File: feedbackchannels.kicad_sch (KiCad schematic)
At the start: 93 parts

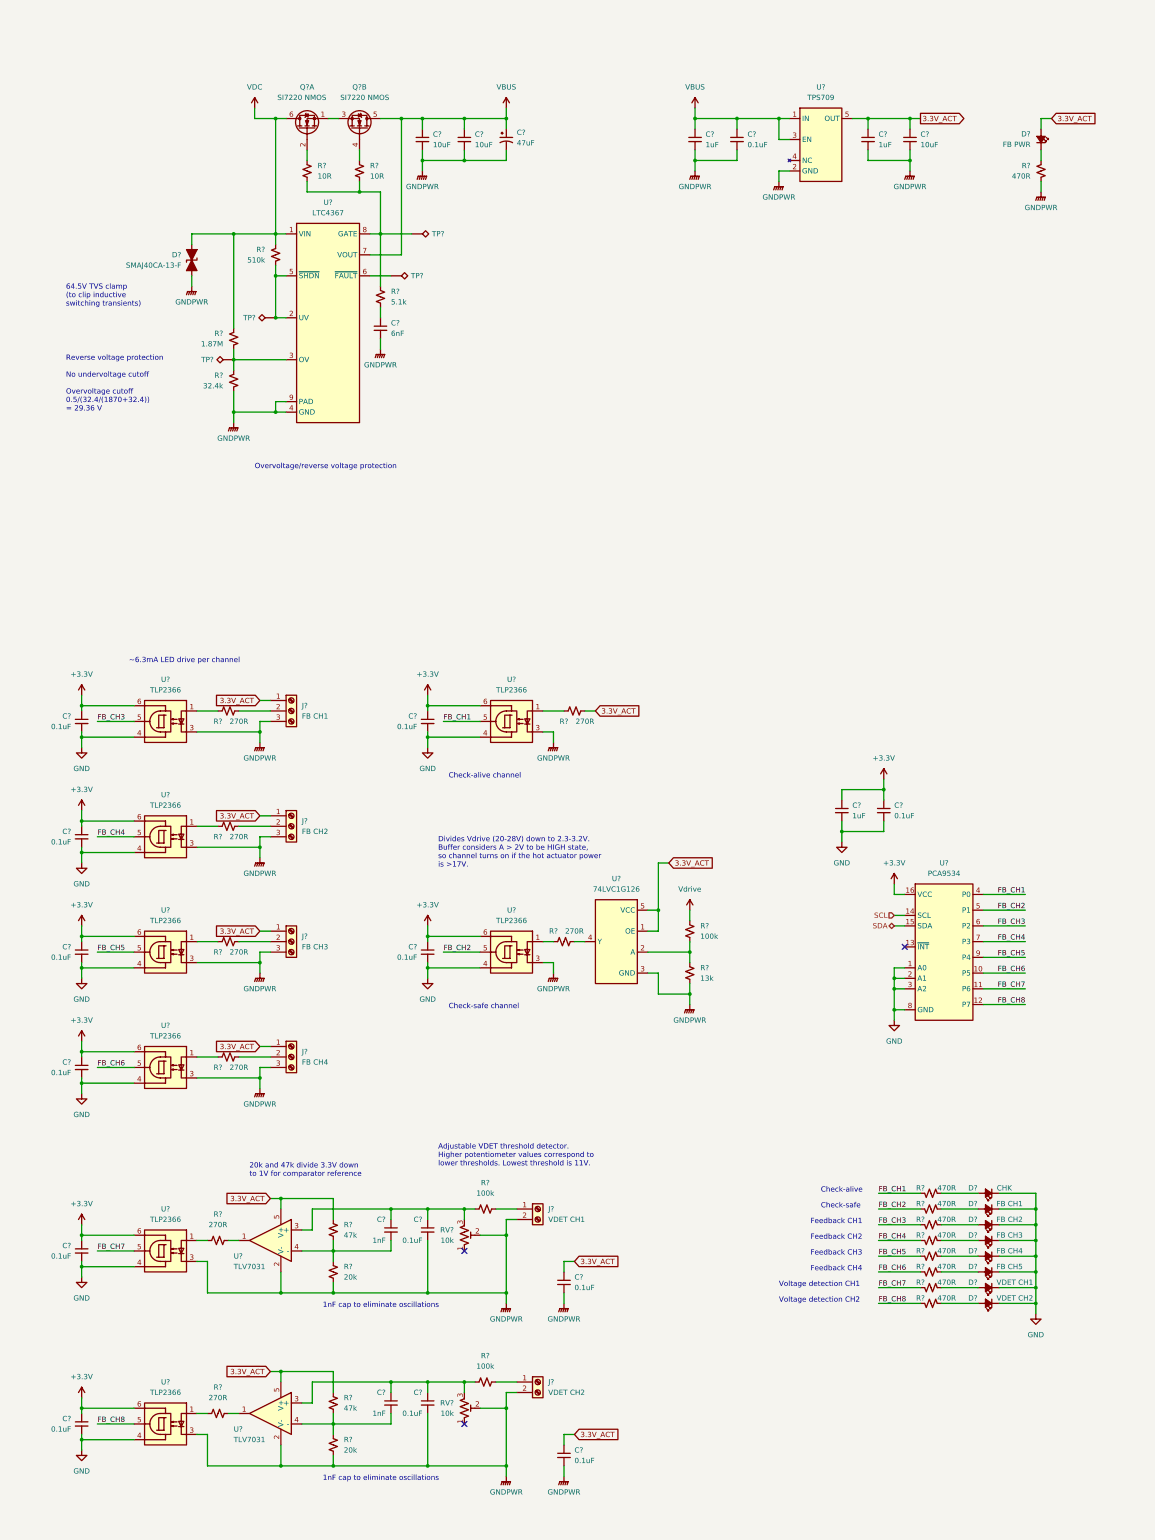
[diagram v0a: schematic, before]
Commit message: Replaced hot-side feedback LDO with buck converter
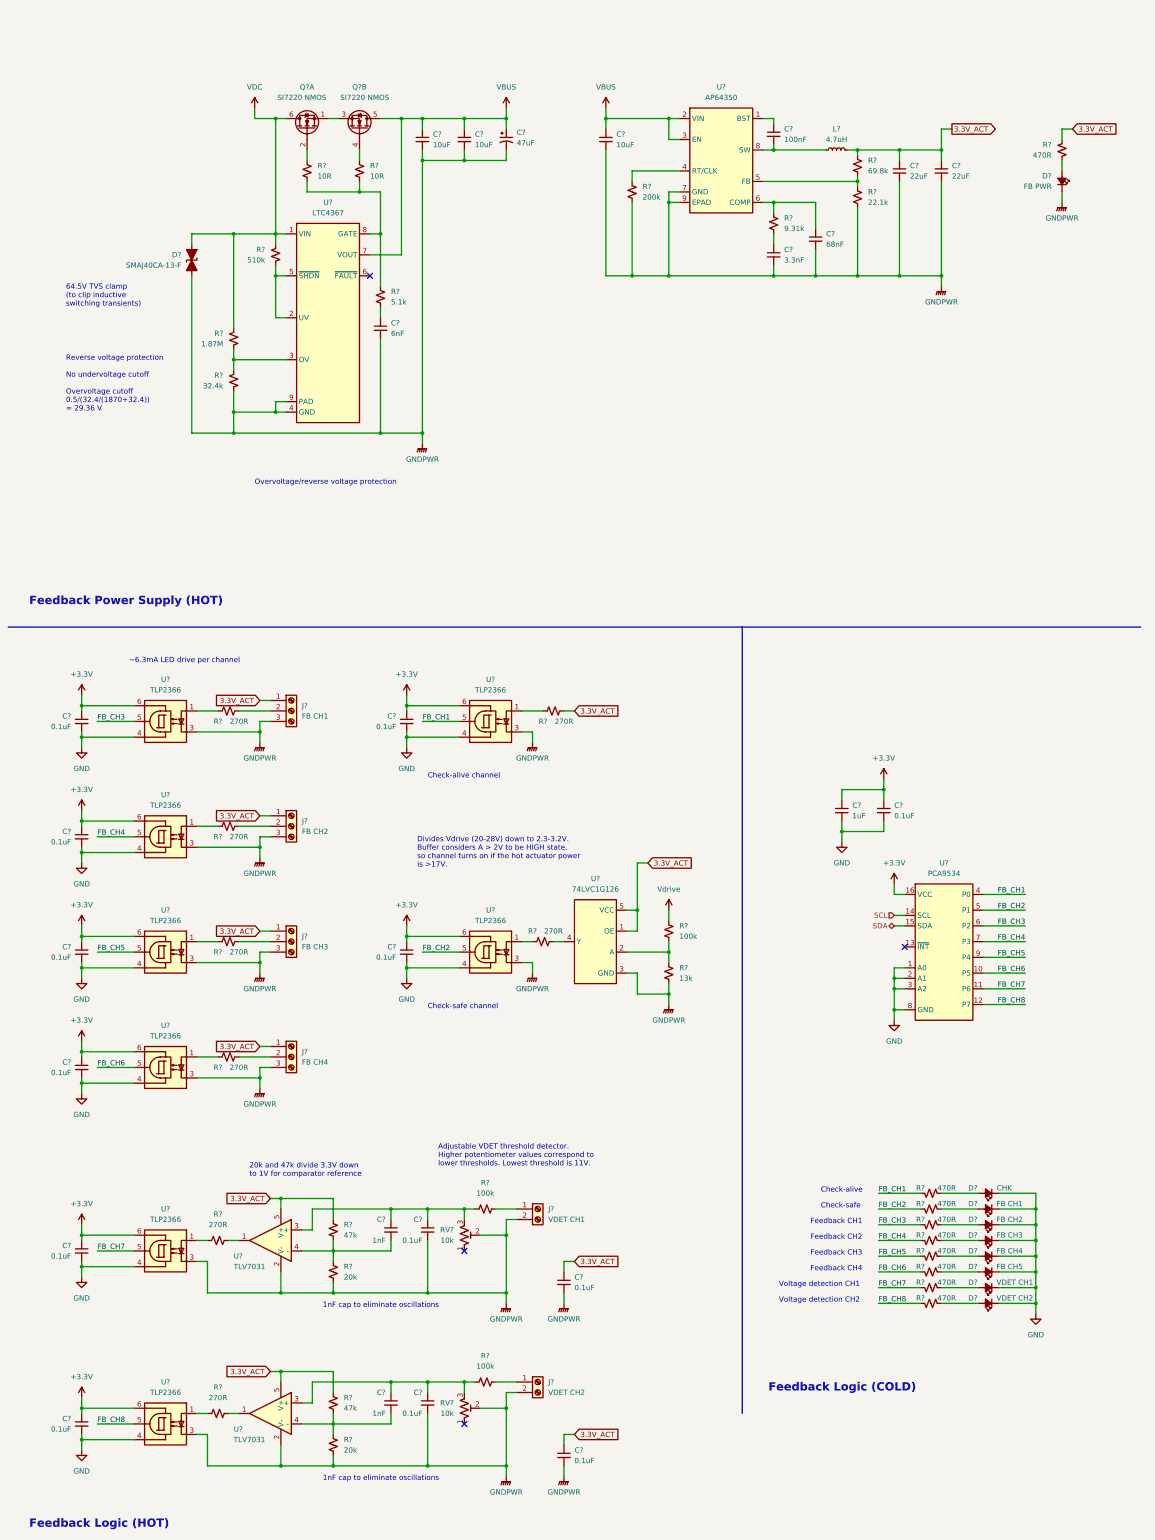
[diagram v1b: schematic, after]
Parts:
- removed C?: 10uF, Capacitor_SMD:C_0603_1608Metric, symbol Device:C_Small
- removed C? (x2): 1uF, Capacitor_SMD:C_0603_1608Metric, symbol Device:C_Small
- removed C?: 0.1uF, Capacitor_SMD:C_0603_1608Metric, symbol Device:C_Small
- removed TP? (x4): TestPoint_Alt, TestPoint:TestPoint_Pad_D2.0mm, symbol Connector:TestPoint_Alt
- removed U?: TPS709, Package_TO_SOT_SMD:SOT-23-5, symbol actuation:TPS709
- added C?: 10uF, symbol Device:C_Small
- added C?: 100nF, symbol Device:C_Small
- added C?: 68nF, symbol Device:C_Small
- added C?: 3.3nF, symbol Device:C_Small
- added C? (x2): 22uF, symbol Device:C_Small
- added L?: 4.7uH, symbol Device:L_Small
- added R?: 200k, symbol Device:R_Small_US
- added R?: 69.8k, symbol Device:R_Small_US
- added R?: 22.1k, symbol Device:R_Small_US
- added R?: 9.31k, symbol Device:R_Small_US
- added U?: AP64350, Package_SO:SOIC-8-1EP_3.9x4.9mm_P1.27mm_EP2.62x3.51mm, symbol actuation:AP64350
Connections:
- net 3.3V_ACT: now also R?.1, C?.1, C?.1, L?.2, R?.1; no longer D?.2 (A)
- net GNDPWR: now also D?.1 (K), C?.2, C?.2, C?.2, C?.2, C?.2, R?.2, R?.2, U?.7 (GND), U?.9 (EPAD); no longer R?.2
- net VBUS: now also C?.1, U?.2 (VIN), U?.3 (EN)
- new net: C?.2, L?.1, U?.8 (SW)
- new net: C?.1, U?.1 (BST)
- new net: R?.1, U?.4 (RT/CLK)
- new net: R?.1, R?.2, U?.5 (FB)
- new net: C?.1, R?.1, U?.6 (COMP)
- new net: C?.1, R?.2
- new net: D?.2 (A), R?.2
- no-connect marks 3 -> 4
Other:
- note added: "Feedback Logic (COLD)"
- note added: "Feedback Logic (HOT)"
- note added: "Feedback Power Supply (HOT)"
- moved on the sheet: C?, D?, R?, U?

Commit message: Reorganizing schematic
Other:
- moved on the sheet: C?, D?, J?, L?, Q?A, Q?B, R?, RV?, U?
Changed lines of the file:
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@@
 (kicad_sch (version 20211123) (generator eeschema)
-  (paper "User" 299.999 399.999)
+  (paper "User" 299.999 380.009)

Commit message: More reorganizing
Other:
- note added: "Feedback Isolators"
- note added: "Feedback Logic"
- note added: "Feedback Power Supply"
- note removed: "Feedback Logic (COLD)"
- note removed: "Feedback Logic (HOT)"
- note removed: "Feedback Power Supply (HOT)"

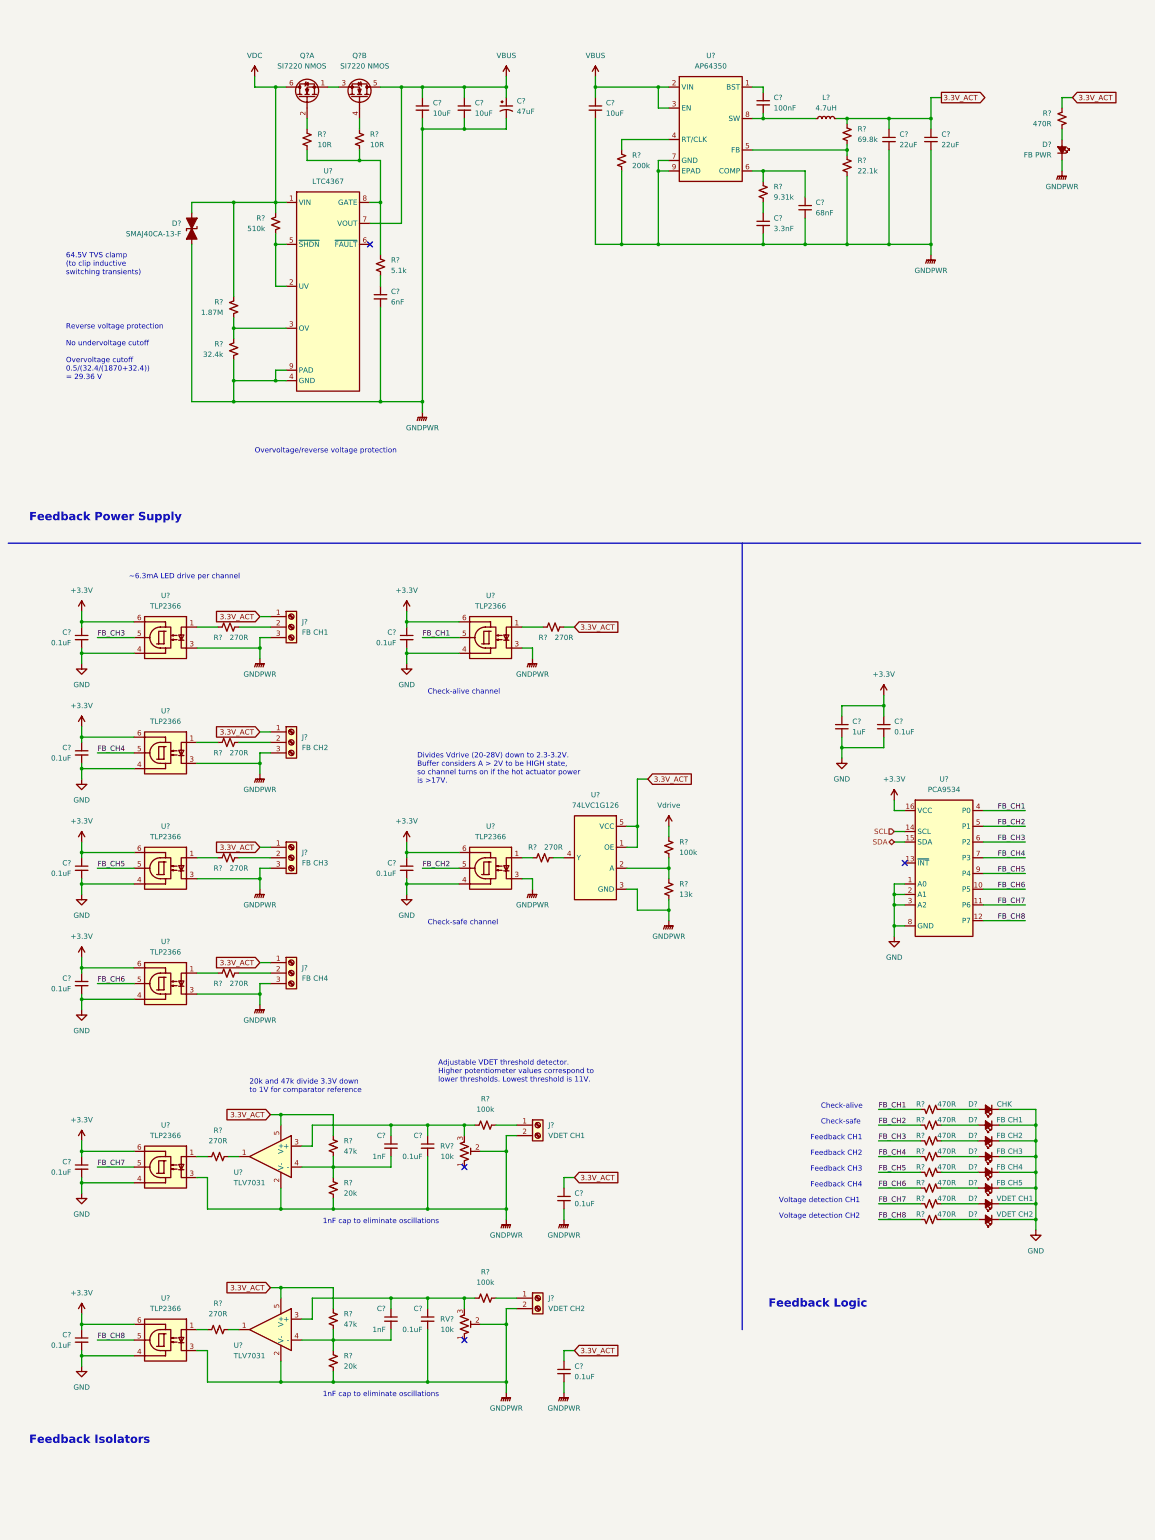
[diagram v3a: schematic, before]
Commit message: Terminal block part selections
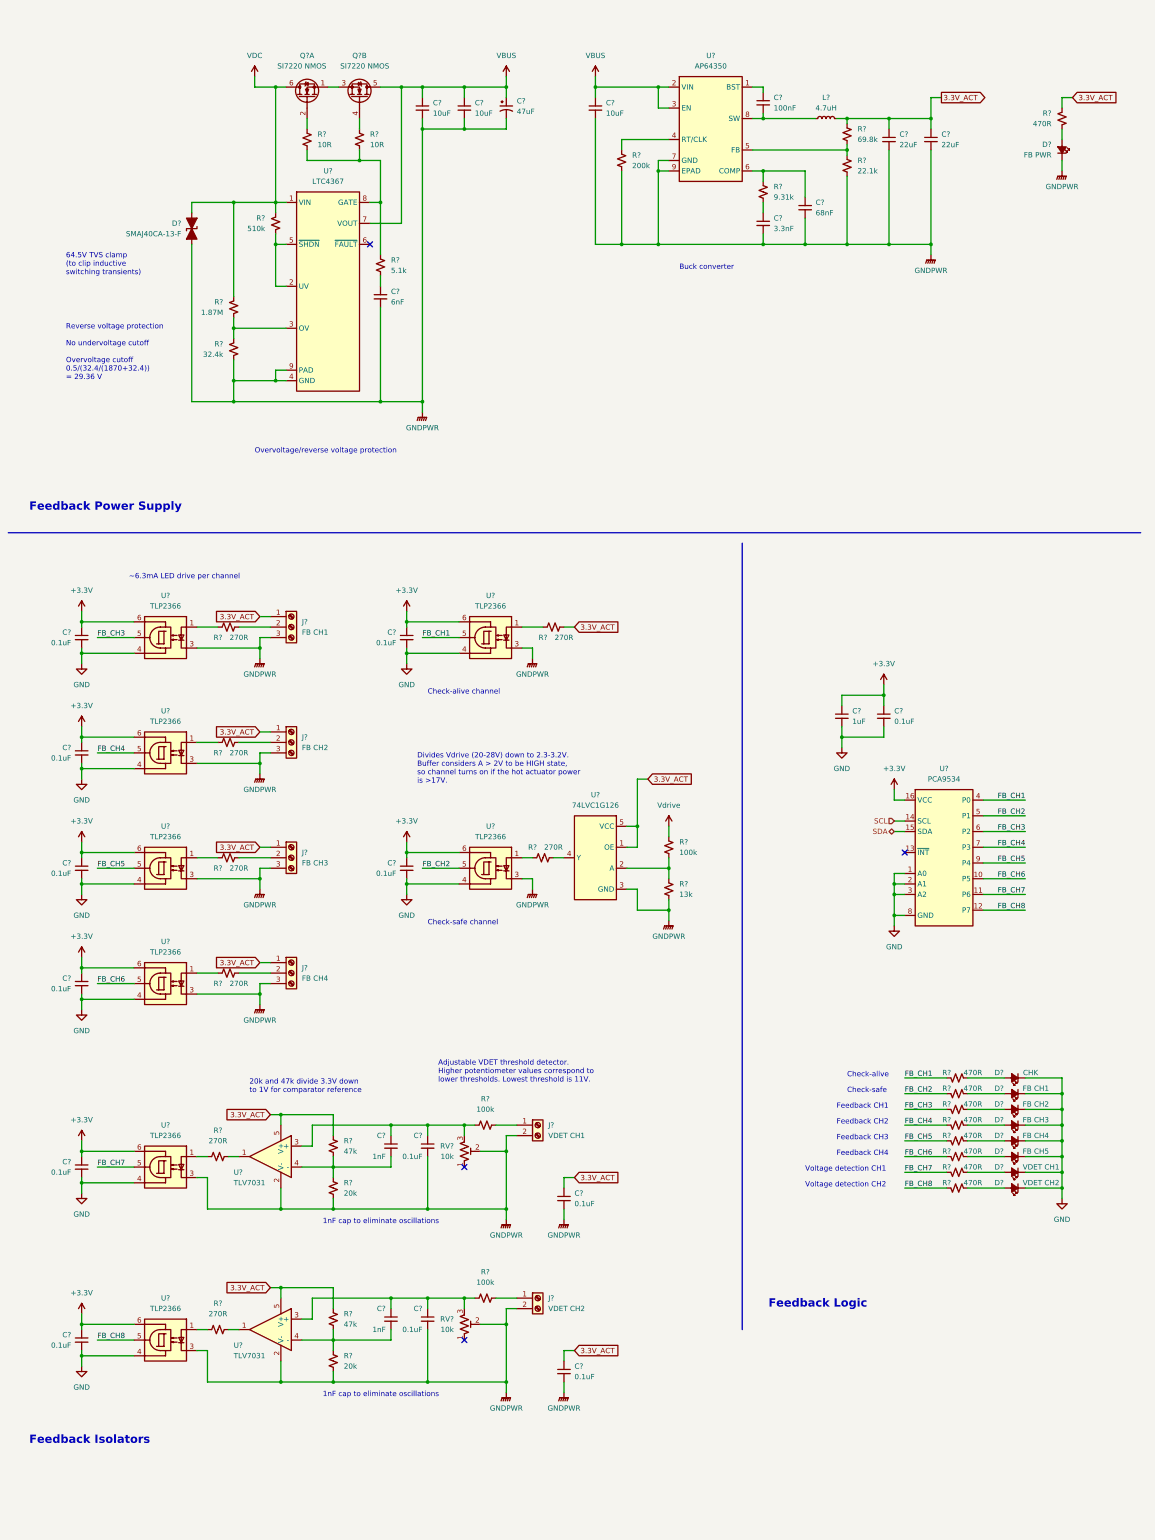
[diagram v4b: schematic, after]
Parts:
- removed J?: FB CH2, symbol Connector:Screw_Terminal_01x03
- removed J?: FB CH3, symbol Connector:Screw_Terminal_01x03
- removed J?: FB CH4, symbol Connector:Screw_Terminal_01x03
- added J?: FB CH4, symbol Connector:Screw_Terminal_01x03
- added J?: FB CH2, symbol Connector:Screw_Terminal_01x03
- added J?: FB CH3, symbol Connector:Screw_Terminal_01x03
- J?: MPN (none) -> 1751251
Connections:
- net 3.3V_ACT: now also J?.1 (Pin_1), J?.1 (Pin_1), J?.1 (Pin_1)
- net GNDPWR: now also J?.3 (Pin_3), J?.3 (Pin_3), J?.3 (Pin_3)
- net at R?.2: now also J?.2 (Pin_2) (x3)
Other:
- note added: "Buck converter"
- moved on the sheet: C?, D?, R?, U?

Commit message: more notes, generate pdf
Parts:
- gave numbers to parts that had none: 95
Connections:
- net +3.3V: now also U34.1 (A0), U34.2 (A1)
- net GND: no longer U34.1 (A0), U34.2 (A1)
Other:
- note added: "I2C address: 0100 A2 A1 A0 Currently wired for 0x23"

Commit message: notes on feedback sheet
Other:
- note added: "200k configures 500kHz switching"
- note added: "Assuming LED forward voltage of 2V, ~2.8mA per"
- note added: "Buck converter for hot-side"
- note added: "Input voltage 3.8-40V (has UVLO), 3.5A output 60-85% efficient at 24V This follows the recommended values for 3.3V"
- note added: "Reverse voltage protection (-40V) No undervoltage cutoff Overvoltage cutoff 0.5/(32.4/(1870+32.4)) = 29.36 V"
- note added: "Set GPIO to high-Z input mode"
- note added: "~6.3mA LED drive per channel at Vf=1.65 Up to 50mA total Output on FB_CHx is 3mA max"
- note removed: "Buck converter"
- note removed: "Reverse voltage protection No undervoltage cutoff Overvoltage cutoff 0.5/(32.4/(1870+32.4)) = 29.36 V"
- note removed: "~6.3mA LED drive per channel"

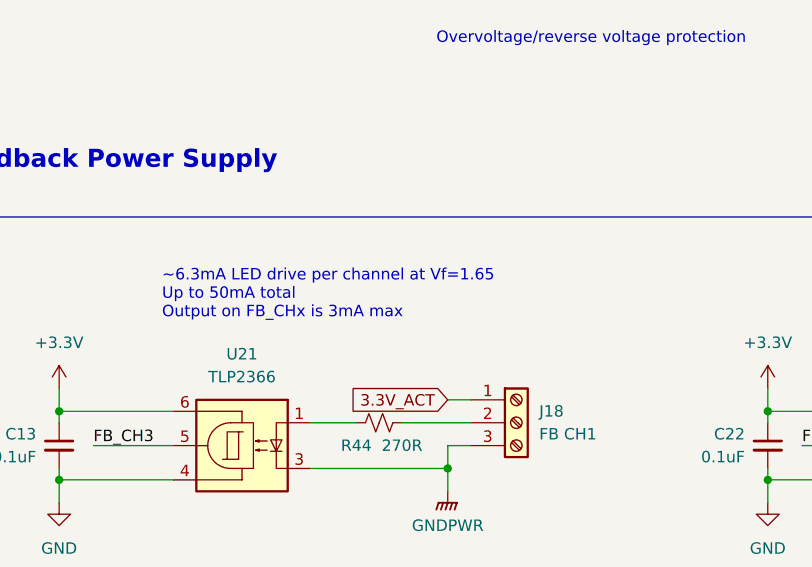
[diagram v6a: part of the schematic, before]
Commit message: estimate 3.3V current consumption
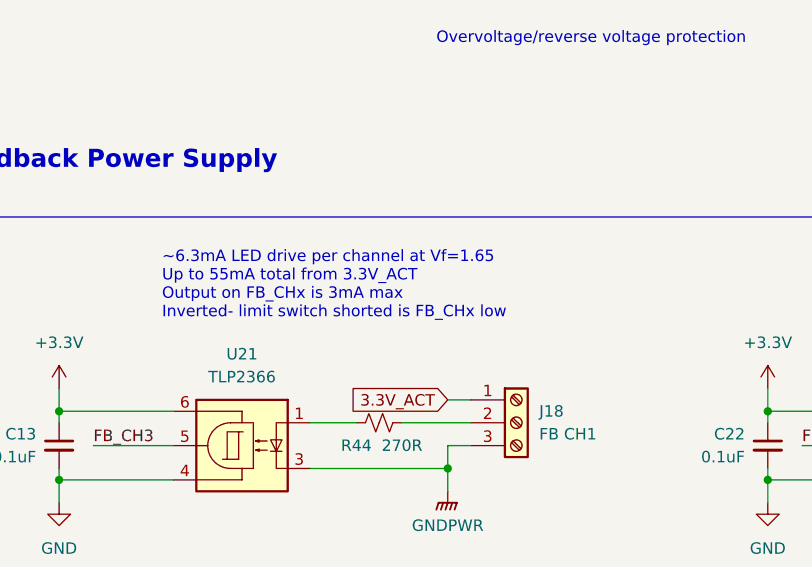
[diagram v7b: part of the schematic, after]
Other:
- note added: "~6.3mA LED drive per channel at Vf=1.65 Up to 55mA total from 3.3V_ACT Output on FB_CHx is 3mA max Inverted- limit switch shorted is FB_CHx low"
- note removed: "~6.3mA LED drive per channel at Vf=1.65 Up to 50mA total Output on FB_CHx is 3mA max"
